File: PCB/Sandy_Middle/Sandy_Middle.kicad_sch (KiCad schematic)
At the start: 82 parts, among them J1 Conn_02x02_Top_Bottom, J2 Conn_02x02_Top_Bottom, J3 Conn_02x02_Top_Bottom

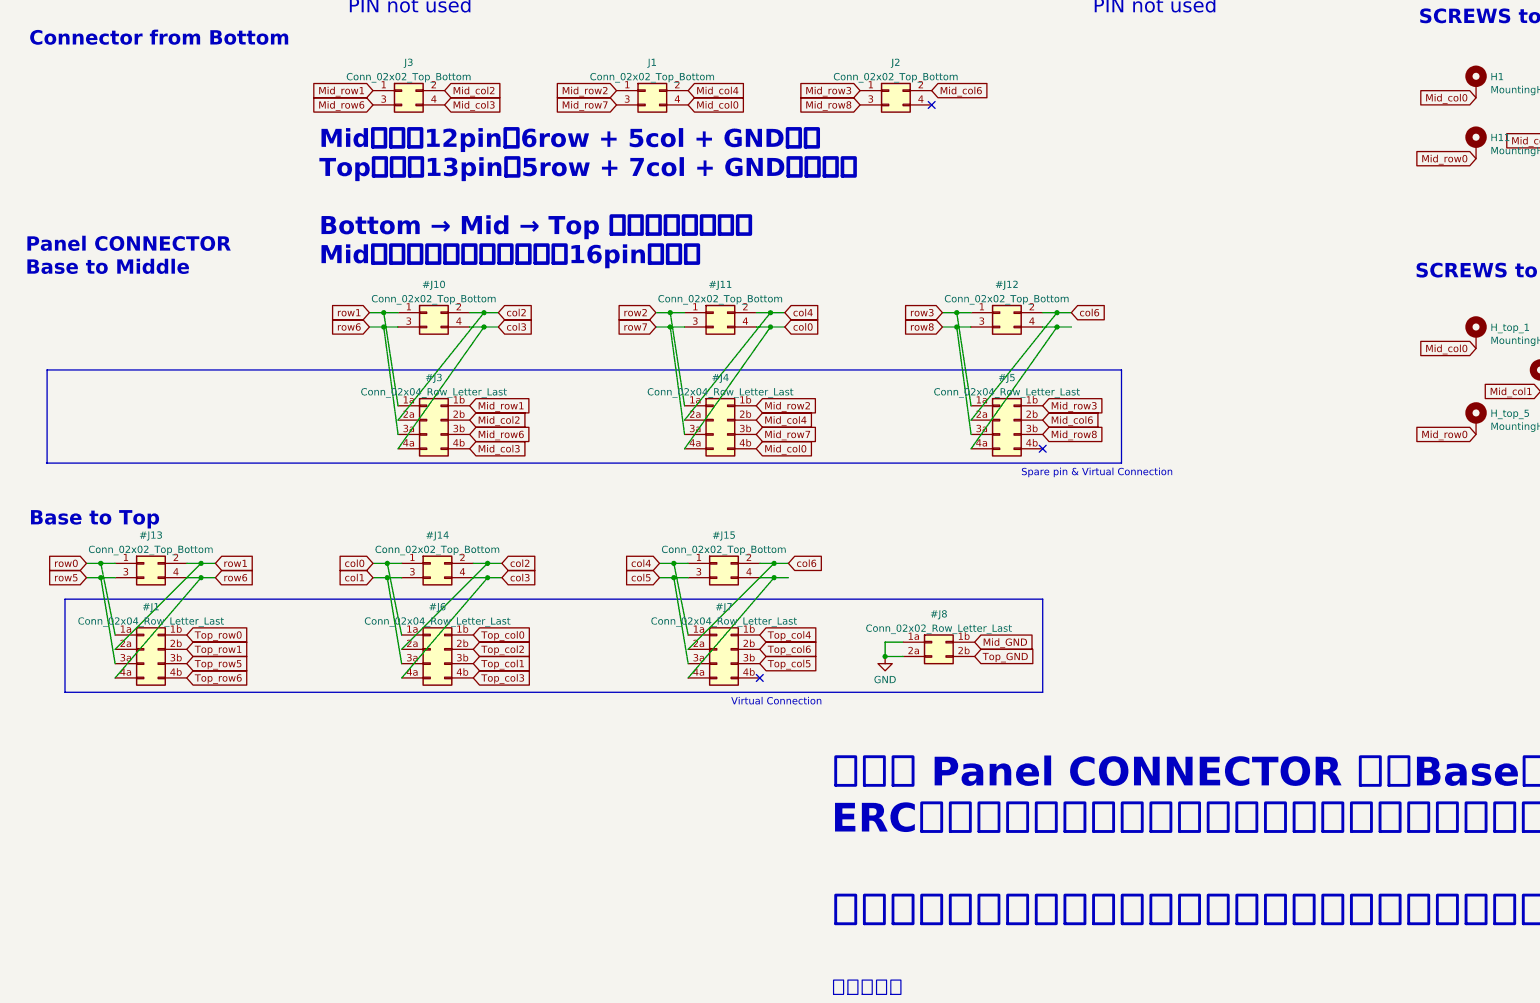
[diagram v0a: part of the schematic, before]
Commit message: SHコネクタで接続するピンを指定
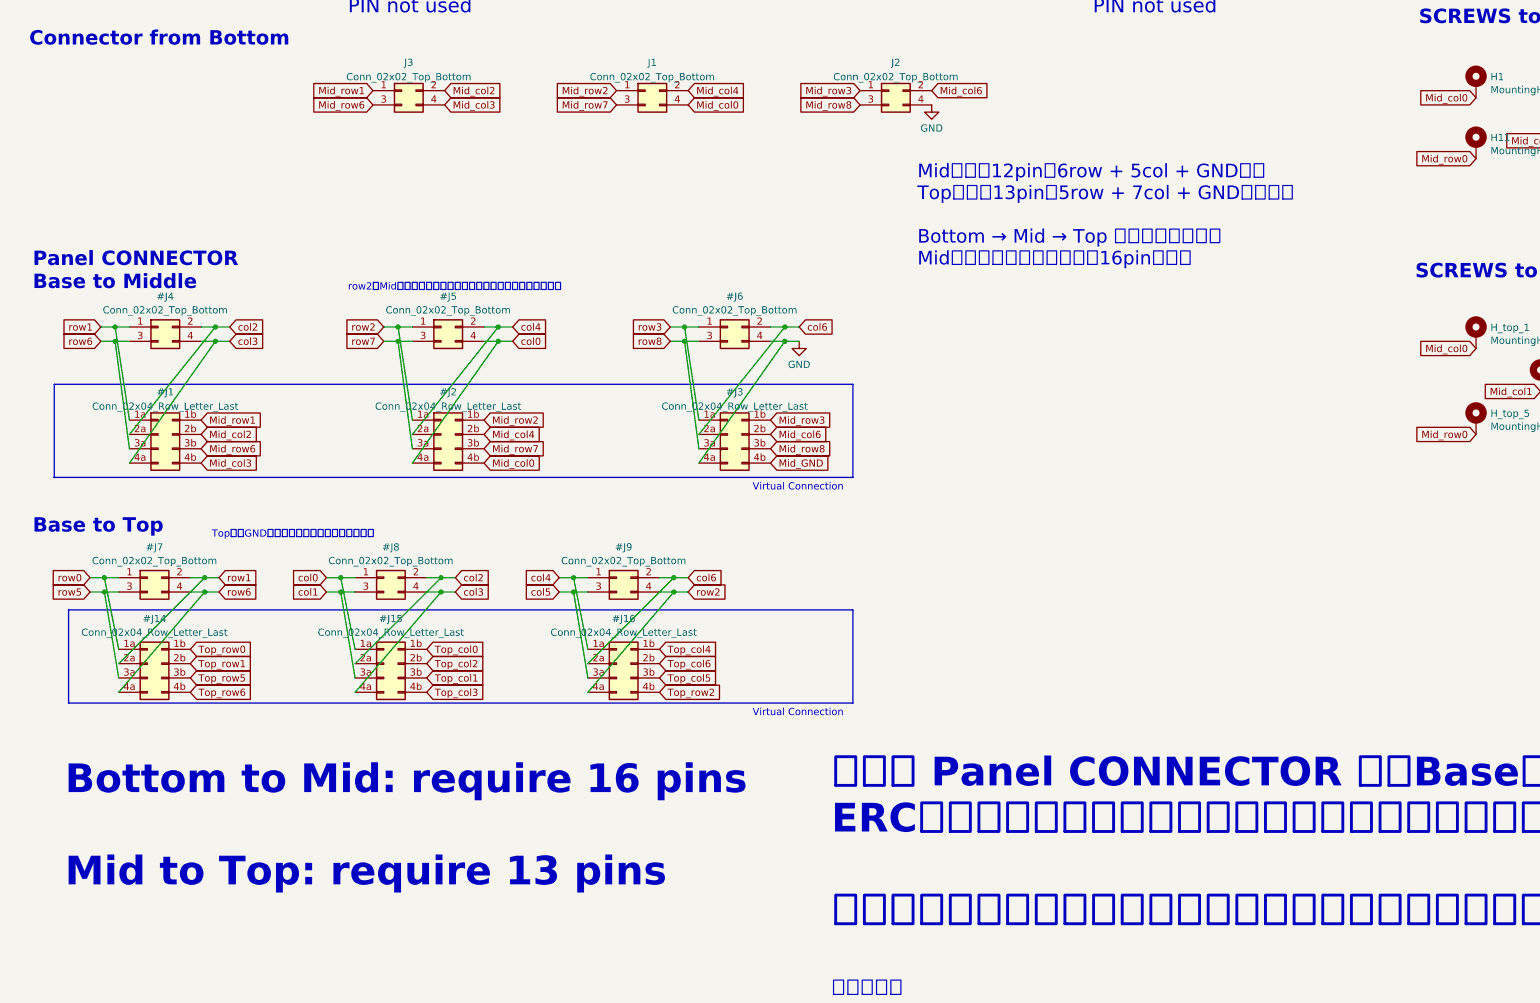
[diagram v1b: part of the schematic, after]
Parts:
- removed #J10, #J11, #J12, #J13, #J14, #J15: Conn_02x02_Top_Bottom, locallib:JST_SH_SM04B-SRSS-TB_1x04-1MP_P1.00mm_Horizontal_wCable_housing_spare_pin, symbol Connector_Generic:Conn_02x02_Odd_Even
- removed #J4, #J5, #J6, #J7: Conn_02x04_Row_Letter_Last, symbol Connector_Generic:Conn_02x04_Row_Letter_Last
- removed #J8: Conn_02x02_Row_Letter_Last, symbol Connector_Generic:Conn_02x02_Row_Letter_Last
- added #J14, #J15, #J16, #J2: Conn_02x04_Row_Letter_Last, symbol Connector_Generic:Conn_02x04_Row_Letter_Last
- added #J4, #J5, #J6, #J7, #J8, #J9: Conn_02x02_Top_Bottom, locallib:JST_SH_SM04B-SRSS-TB_1x04-1MP_P1.00mm_Horizontal_wCable_housing_spare_pin_courtyard, symbol Connector_Generic:Conn_02x02_Odd_Even
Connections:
- net GND: now also #J3.4a (Pin_4a), J2.4 (Pin_4), #J6.4 (Pin_4)
- net Mid_GND: now also #J3.4b (Pin_4b)
- net Mid_col0: now also #J2.4b (Pin_4b)
- net Mid_col2: now also #J1.2b (Pin_2b); no longer #J3.2b (Pin_2b)
- net Mid_col3: now also #J1.4b (Pin_4b); no longer #J3.4b (Pin_4b)
- net Mid_col4: now also #J2.2b (Pin_2b)
- net Mid_col6: now also #J3.2b (Pin_2b)
- net Mid_row1: now also #J1.1b (Pin_1b); no longer #J3.1b (Pin_1b)
- net Mid_row2: now also #J2.1b (Pin_1b)
- net Mid_row3: now also #J3.1b (Pin_1b)
- net Mid_row6: now also #J1.3b (Pin_3b); no longer #J3.3b (Pin_3b)
- net Mid_row7: now also #J2.3b (Pin_3b)
- net Mid_row8: now also #J3.3b (Pin_3b)
- net Top_col0: now also #J15.1b (Pin_1b)
- net Top_col1: now also #J15.3b (Pin_3b)
- net Top_col2: now also #J15.2b (Pin_2b)
- net Top_col3: now also #J15.4b (Pin_4b)
- net Top_col4: now also #J16.1b (Pin_1b)
- net Top_col5: now also #J16.3b (Pin_3b)
- net Top_col6: now also #J16.2b (Pin_2b)
- net Top_row0: now also #J14.1b (Pin_1b); no longer #J1.1b (Pin_1b)
- net Top_row1: now also #J14.2b (Pin_2b); no longer #J1.2b (Pin_2b)
- net Top_row5: now also #J14.3b (Pin_3b); no longer #J1.3b (Pin_3b)
- net Top_row6: now also #J14.4b (Pin_4b); no longer #J1.4b (Pin_4b)
- net col0: now also #J15.1a (Pin_1a), #J2.4a (Pin_4a), #J5.4 (Pin_4), #J8.1 (Pin_1)
- net col1: now also #J15.3a (Pin_3a), #J8.3 (Pin_3)
- net col2: now also #J1.2a (Pin_2a), #J15.2a (Pin_2a), #J4.2 (Pin_2), #J8.2 (Pin_2); no longer #J3.2a (Pin_2a)
- net col3: now also #J1.4a (Pin_4a), #J15.4a (Pin_4a), #J4.4 (Pin_4), #J8.4 (Pin_4); no longer #J3.4a (Pin_4a)
- net col4: now also #J16.1a (Pin_1a), #J2.2a (Pin_2a), #J5.2 (Pin_2), #J9.1 (Pin_1)
- net col5: now also #J16.3a (Pin_3a), #J9.3 (Pin_3)
- net col6: now also #J3.2a (Pin_2a), #J16.2a (Pin_2a), #J6.2 (Pin_2), #J9.2 (Pin_2)
- net row0: now also #J14.1a (Pin_1a), #J7.1 (Pin_1); no longer #J1.1a (Pin_1a)
- net row1: now also #J1.1a (Pin_1a), #J14.2a (Pin_2a), #J4.1 (Pin_1), #J7.2 (Pin_2); no longer #J1.2a (Pin_2a), #J3.1a (Pin_1a)
- net row2: now also #J16.4a (Pin_4a), #J2.1a (Pin_1a), #J5.1 (Pin_1), #J9.4 (Pin_4)
- net row3: now also #J3.1a (Pin_1a), #J6.1 (Pin_1)
- net row5: now also #J14.3a (Pin_3a), #J7.3 (Pin_3); no longer #J1.3a (Pin_3a)
- net row6: now also #J1.3a (Pin_3a), #J14.4a (Pin_4a), #J4.3 (Pin_3), #J7.4 (Pin_4); no longer #J1.4a (Pin_4a), #J3.3a (Pin_3a)
- net row7: now also #J2.3a (Pin_3a), #J5.3 (Pin_3)
- net row8: now also #J3.3a (Pin_3a), #J6.3 (Pin_3)
- new net Top_row2: #J16.4b (Pin_4b)
- no-connect marks 3 -> 0
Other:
- note added: "Bottom to Mid: require 16 pins Mid to Top: require 13 pins"
- note added: "TopへはGNDも送りたいが、ピンが足りない。"
- note added: "row2はMidで使用していないが、ピンが余っているので追加。"
- note removed: "Spare pin & Virtual Connection"

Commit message: WIP シルクがハンダマスクに切り取られる箇所をフットプリントを変更して対応
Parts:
- EXT_MC0, EXT_MC1, EXT_MC2, EXT_MC3, EXT_MC4, EXT_MC5, EXT_MC6, EXT_MR0, EXT_MR1, EXT_MR2, EXT_MR3, EXT_MR5, EXT_MR6, EXT_MR7, EXT_MR8: footprint TestPoint:TestPoint_THTPad_D2.0mm_Drill1.0mm -> locallib:TestPoint_THTPad_D2.0mm_Drill1.0mm
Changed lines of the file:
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@@
 			)
 		)
-		(property "Footprint" "TestPoint:TestPoint_THTPad_D2.0mm_Drill1.0mm"
+		(property "Footprint" "locallib:TestPoint_THTPad_D2.0mm_Drill1.0mm"
 			(at 137.16 156.21 0)
 			(effects
@@
 			)
 		)
-		(property "Footprint" "TestPoint:TestPoint_THTPad_D2.0mm_Drill1.0mm"
+		(property "Footprint" "locallib:TestPoint_THTPad_D2.0mm_Drill1.0mm"
 			(at 284.48 118.11 0)
 			(effects
@@
 			)
 		)
-		(property "Footprint" "TestPoint:TestPoint_THTPad_D2.0mm_Drill1.0mm"
+		(property "Footprint" "locallib:TestPoint_THTPad_D2.0mm_Drill1.0mm"
 			(at 284.48 52.07 0)
 			(effects
@@
 			)
 		)
-		(property "Footprint" "TestPoint:TestPoint_THTPad_D2.0mm_Drill1.0mm"
+		(property "Footprint" "locallib:TestPoint_THTPad_D2.0mm_Drill1.0mm"
 			(at 284.48 83.82 0)
 			(effects
@@
 			)
 		)
-		(property "Footprint" "TestPoint:TestPoint_THTPad_D2.0mm_Drill1.0mm"
+		(property "Footprint" "locallib:TestPoint_THTPad_D2.0mm_Drill1.0mm"
 			(at 71.12 156.21 0)
 			(effects
@@
 			)
 		)
-		(property "Footprint" "TestPoint:TestPoint_THTPad_D2.0mm_Drill1.0mm"
+		(property "Footprint" "locallib:TestPoint_THTPad_D2.0mm_Drill1.0mm"
 			(at 284.48 147.32 0)
 			(effects
@@
 			)
 		)
-		(property "Footprint" "TestPoint:TestPoint_THTPad_D2.0mm_Drill1.0mm"
+		(property "Footprint" "locallib:TestPoint_THTPad_D2.0mm_Drill1.0mm"
 			(at 284.48 115.57 0)
 			(effects
@@
 			)
 		)
-		(property "Footprint" "TestPoint:TestPoint_THTPad_D2.0mm_Drill1.0mm"
+		(property "Footprint" "locallib:TestPoint_THTPad_D2.0mm_Drill1.0mm"
 			(at 38.1 156.21 0)
 			(effects
@@
 			)
 		)
-		(property "Footprint" "TestPoint:TestPoint_THTPad_D2.0mm_Drill1.0mm"
+		(property "Footprint" "locallib:TestPoint_THTPad_D2.0mm_Drill1.0mm"
 			(at 284.48 54.61 0)
 			(effects
@@
 			)
 		)
-		(property "Footprint" "TestPoint:TestPoint_THTPad_D2.0mm_Drill1.0mm"
+		(property "Footprint" "locallib:TestPoint_THTPad_D2.0mm_Drill1.0mm"
 			(at 284.48 86.36 0)
 			(effects
@@
 			)
 		)
-		(property "Footprint" "TestPoint:TestPoint_THTPad_D2.0mm_Drill1.0mm"
+		(property "Footprint" "locallib:TestPoint_THTPad_D2.0mm_Drill1.0mm"
 			(at 203.2 156.21 0)
 			(effects
@@
 			)
 		)
-		(property "Footprint" "TestPoint:TestPoint_THTPad_D2.0mm_Drill1.0mm"
+		(property "Footprint" "locallib:TestPoint_THTPad_D2.0mm_Drill1.0mm"
 			(at 104.14 156.21 0)
 			(effects
@@
 			)
 		)
-		(property "Footprint" "TestPoint:TestPoint_THTPad_D2.0mm_Drill1.0mm"
+		(property "Footprint" "locallib:TestPoint_THTPad_D2.0mm_Drill1.0mm"
 			(at 284.48 149.86 0)
 			(effects
@@
 			)
 		)
-		(property "Footprint" "TestPoint:TestPoint_THTPad_D2.0mm_Drill1.0mm"
+		(property "Footprint" "locallib:TestPoint_THTPad_D2.0mm_Drill1.0mm"
 			(at 170.18 156.21 0)
 			(effects
@@
 			)
 		)
-		(property "Footprint" "TestPoint:TestPoint_THTPad_D2.0mm_Drill1.0mm"
+		(property "Footprint" "locallib:TestPoint_THTPad_D2.0mm_Drill1.0mm"
 			(at 236.22 156.21 0)
 			(effects

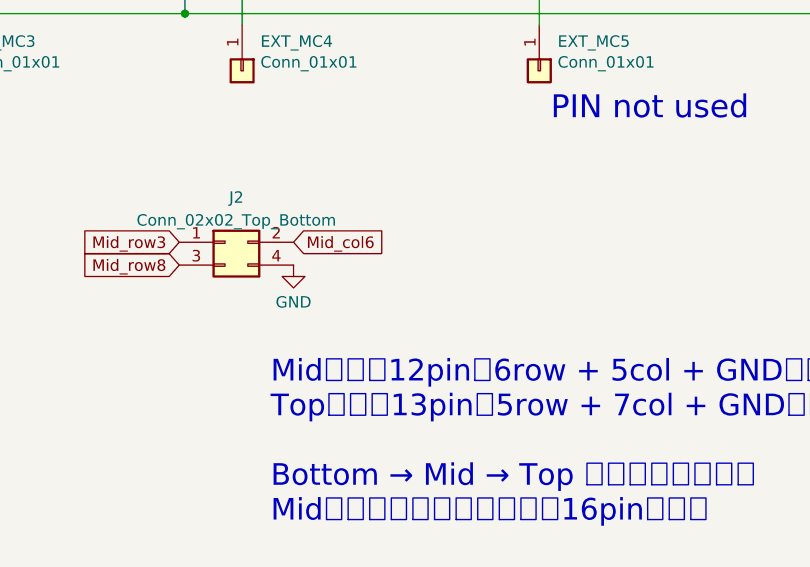
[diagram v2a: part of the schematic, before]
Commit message: GNDとMid_GNDを接続
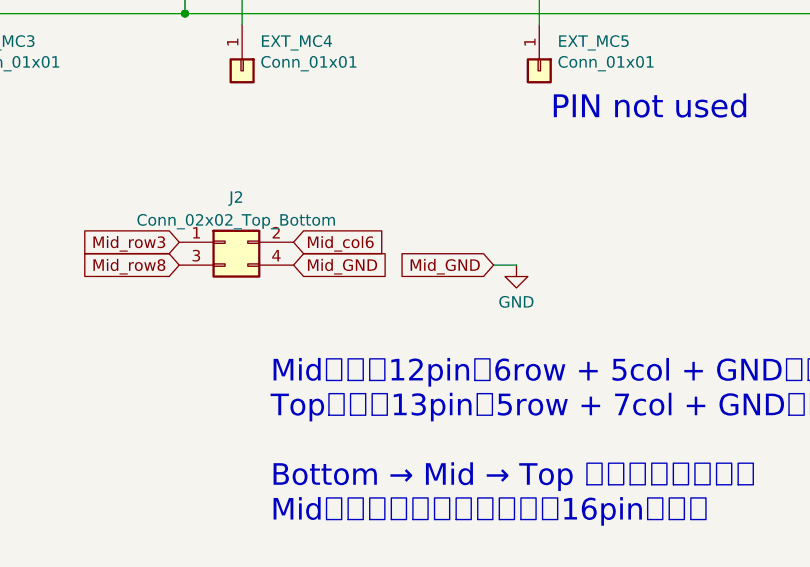
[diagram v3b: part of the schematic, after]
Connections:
- net Mid_GND is gone; now on net GND: #J3.4b (Pin_4b), H12.1, H_top_10.1
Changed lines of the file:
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@@
 	(wire
 		(pts
+			(xy 198.12 177.8) (xy 200.66 177.8)
+		)
+		(stroke
+			(width 0)
+			(type default)
+		)
+	)
+	(wire
+		(pts
 			(xy 236.22 31.75) (xy 236.22 74.93)
 		)
@@
 		)
 	)
+	(global_label "Mid_GND"
+		(shape input)
+		(at 198.12 177.8 180)
+		(fields_autoplaced yes)
+		(effects
+			(font
+				(size 1.27 1.27)
+			)
+			(justify right)
+		)
+		(property "Intersheetrefs" "${INTERSHEET_REFS}"
+			(at 187.7457 177.8 0)
+			(effects
+				(font
+					(size 1.27 1.27)
+				)
+				(justify right)
+				(hide yes)
+			)
+		)
+		(property "シート間のリファレンス" "${INTERSHEET_REFS}"
+			(at 198.12 179.6352 0)
+			(effects
+				(font
+					(size 1.27 1.27)
+				)
+				(justify right)
+				(hide yes)
+			)
+		)
+	)
 	(global_label "Mid_row2"
 		(shape input)
@@
 		)
 	)
+	(global_label "Mid_GND"
+		(shape input)
+		(at 175.895 177.8 0)
+		(fields_autoplaced yes)
+		(effects
+			(font
+				(size 1.27 1.27)
+			)
+			(justify left)
+		)
+		(property "Intersheetrefs" "${INTERSHEET_REFS}"
+			(at 186.2693 177.8 0)
+			(effects
+				(font
+					(size 1.27 1.27)
+				)
+				(justify left)
+				(hide yes)
+			)
+		)
+		(property "シート間のリファレンス" "${INTERSHEET_REFS}"
+			(at 175.895 179.6352 0)
+			(effects
+				(font
+					(size 1.27 1.27)
+				)
+				(justify left)
+				(hide yes)
+			)
+		)
+	)
 	(global_label "Mid_col5"
 		(shape input)
@@
 	(symbol
 		(lib_id "power:GND")
-		(at 175.895 177.8 0)
+		(at 200.66 177.8 0)
 		(unit 1)
 		(exclude_from_sim no)
@@
 		(fields_autoplaced yes)
 		(property "Reference" "#PWR03"
-			(at 175.895 184.15 0)
+			(at 200.66 184.15 0)
 			(effects
 				(font
@@
 		)
 		(property "Value" "GND"
-			(at 175.895 181.9331 0)
+			(at 200.66 181.9331 0)
 			(effects
 				(font
@@
 		)
 		(property "Footprint" ""
-			(at 175.895 177.8 0)
+			(at 200.66 177.8 0)
 			(effects
 				(font
@@
 		)
 		(property "Datasheet" ""
-			(at 175.895 177.8 0)
+			(at 200.66 177.8 0)
 			(effects
 				(font
@@
 		)
 		(property "Description" "Power symbol creates a global label with name \"GND\" , ground"
-			(at 175.895 177.8 0)
+			(at 200.66 177.8 0)
 			(effects
 				(font

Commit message: WIP Choc V2のフットプリントに変更。配置考え中。
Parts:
- SW_BS1: footprint MX_Alps_Hybrid:MXOnly-1U-Hotswap-screw-hole-side1-guide -> locallib:Kailh_socket_ChocV2
- SW_G1, SW_H1, SW_P1, SW_Q1, SW_R1, SW_R4CNT_C1, SW_R4CNT_L1, SW_R4CNT_R1, SW_TAB1, SW_U1: footprint MX_Alps_Hybrid:MXOnly-1U-Hotswap-guide -> locallib:Kailh_socket_ChocV2
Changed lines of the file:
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@@
 			)
 		)
-		(property "Footprint" "MX_Alps_Hybrid:MXOnly-1U-Hotswap-screw-hole-side1-guide"
+		(property "Footprint" "locallib:Kailh_socket_ChocV2"
 			(at 257.81 69.85 0)
 			(effects
@@
 			)
 		)
-		(property "Footprint" "MX_Alps_Hybrid:MXOnly-1U-Hotswap-guide"
+		(property "Footprint" "locallib:Kailh_socket_ChocV2"
 			(at 158.75 101.6 0)
 			(effects
@@
 			)
 		)
-		(property "Footprint" "MX_Alps_Hybrid:MXOnly-1U-Hotswap-guide"
+		(property "Footprint" "locallib:Kailh_socket_ChocV2"
 			(at 109.22 69.85 0)
 			(effects
@@
 			)
 		)
-		(property "Footprint" "MX_Alps_Hybrid:MXOnly-1U-Hotswap-guide"
+		(property "Footprint" "locallib:Kailh_socket_ChocV2"
 			(at 241.3 69.85 0)
 			(effects
@@
 			)
 		)
-		(property "Footprint" "MX_Alps_Hybrid:MXOnly-1U-Hotswap-guide"
+		(property "Footprint" "locallib:Kailh_socket_ChocV2"
 			(at 59.69 69.85 0)
 			(effects
@@
 			)
 		)
-		(property "Footprint" "MX_Alps_Hybrid:MXOnly-1U-Hotswap-guide"
+		(property "Footprint" "locallib:Kailh_socket_ChocV2"
 			(at 175.26 133.35 0)
 			(effects
@@
 			)
 		)
-		(property "Footprint" "MX_Alps_Hybrid:MXOnly-1U-Hotswap-guide"
+		(property "Footprint" "locallib:Kailh_socket_ChocV2"
 			(at 191.77 69.85 0)
 			(effects
@@
 			)
 		)
-		(property "Footprint" "MX_Alps_Hybrid:MXOnly-1U-Hotswap-guide"
+		(property "Footprint" "locallib:Kailh_socket_ChocV2"
 			(at 125.73 101.6 0)
 			(effects
@@
 			)
 		)
-		(property "Footprint" "MX_Alps_Hybrid:MXOnly-1U-Hotswap-guide"
+		(property "Footprint" "locallib:Kailh_socket_ChocV2"
 			(at 43.18 69.85 0)
 			(effects
@@
 			)
 		)
-		(property "Footprint" "MX_Alps_Hybrid:MXOnly-1U-Hotswap-guide"
+		(property "Footprint" "locallib:Kailh_socket_ChocV2"
 			(at 125.73 133.35 0)
 			(effects
@@
 			)
 		)
-		(property "Footprint" "MX_Alps_Hybrid:MXOnly-1U-Hotswap-guide"
+		(property "Footprint" "locallib:Kailh_socket_ChocV2"
 			(at 142.24 133.35 0)
 			(effects

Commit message: WIP 4行化
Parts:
- removed EXT_MR3, EXT_MR7, EXT_MR8: Conn_01x01, locallib:TestPoint_THTPad_D2.0mm_Drill1.0mm, symbol Connector_Generic:Conn_01x01
- added EXT_MR4: Conn_01x01, locallib:TestPoint_THTPad_D2.0mm_Drill1.0mm, symbol Connector_Generic:Conn_01x01
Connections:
- net row8 is gone; now on net row5: #J3.3a (Pin_3a), #J6.3 (Pin_3)
- net GND: no longer H12.1, H_top_10.1
- net Mid_col3: no longer SW_H1.1
- net Mid_col4: now also SW_H1.1
- net Mid_row0: now also D1.1 (K), D3.1 (K), D5.1 (K)
- net Mid_row1: now also D9.1 (K); no longer D1.1 (K), D3.1 (K), D5.1 (K)
- net Mid_row2: now also D12.1 (K), D13.1 (K)
- net Mid_row3: no longer D12.1 (K), D13.1 (K)
- net Mid_row5: now also #J3.3b (Pin_3b), D7.1 (K), J2.3 (Pin_3)
- net Mid_row6: now also D11.1 (K); no longer D2.1 (K), D4.1 (K), D6.1 (K)
- net Mid_row7: no longer D7.1 (K), D9.1 (K), H14.1
- removed net Mid_row8: #J3.3b (Pin_3b), D11.1 (K), H16.1, J2.3 (Pin_3)
- new net Mid_GND: H12.1, H_top_10.1
- new net Mid_row4: D2.1 (K), D4.1 (K), D6.1 (K), EXT_MR4.1 (Pin_1)
- no-connect marks 0 -> 2
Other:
- note removed: "PIN not used"
- note removed: "PINs not used"
- note removed: "SW_H1は、本来 Col4 → Row2 に配置されるが、 Top基板への接続本数を減らすため、隣へ移動。"
- moved on the sheet: D1, D11, D12, D13, D2, D3, D4, D5, D6, D7, D9, EXT_MC0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
